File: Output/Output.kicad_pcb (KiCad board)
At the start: 2 copper layers, 118 x 51.5 mm, 22 parts, among them J1 Conn_01x10_Pin, J2 Conn_01x04_Pin, J3 Conn_01x03_Pin, J4 Conn_01x02_Pin, J5 Conn_01x01_Pin, U10 HDSP-7403, U11 ATMEGA328-PU, U2 74LS273, U3 74HC595, U4 HDSP-7403, U5 74HC595, U6 HDSP-7403, U7 74HC595, U8 HDSP-7403, U9 74HC595, Y1 16MHz

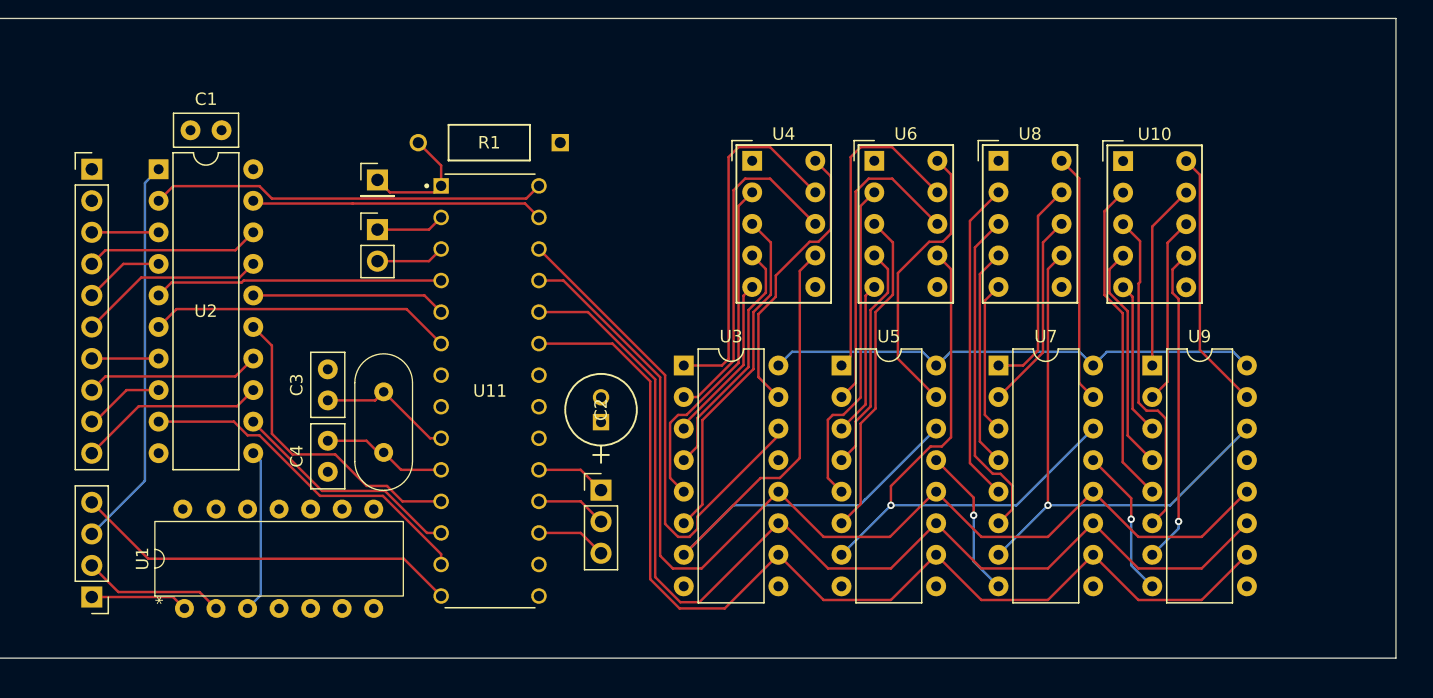
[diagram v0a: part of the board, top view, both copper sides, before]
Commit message: Output PCB routed
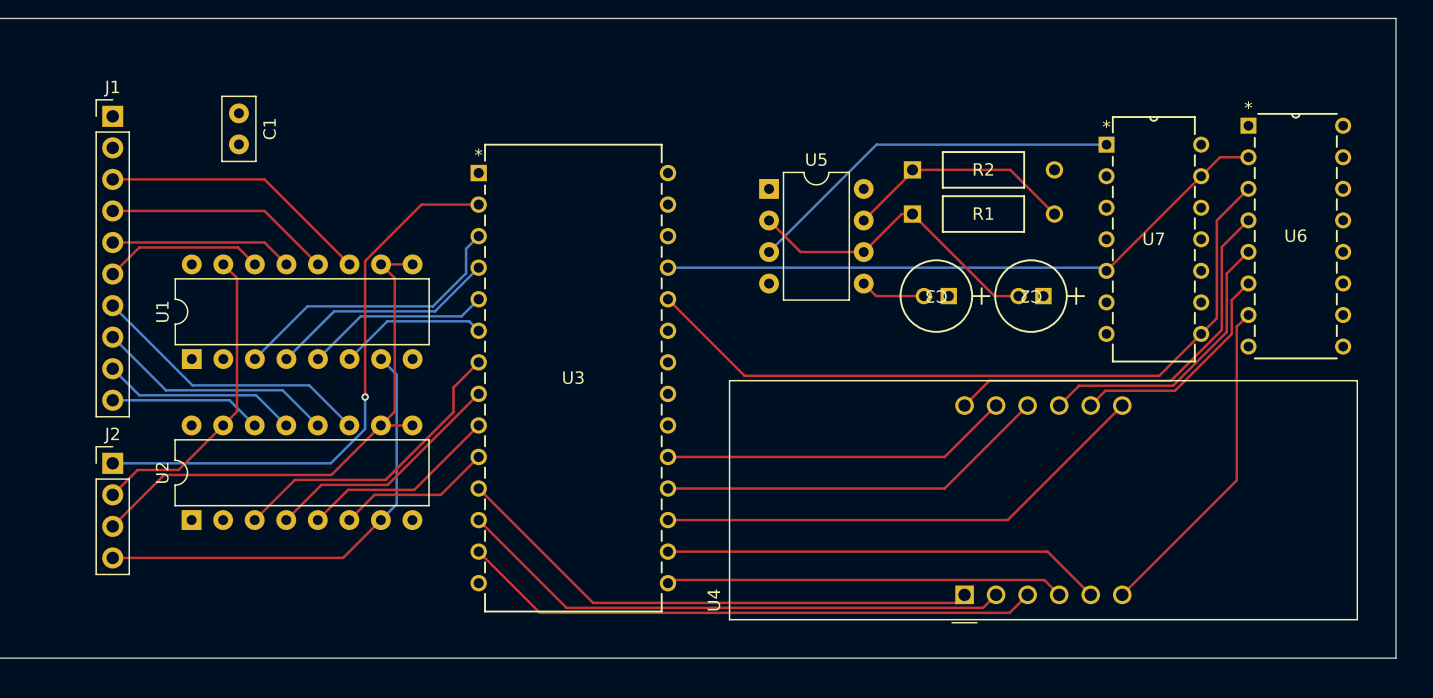
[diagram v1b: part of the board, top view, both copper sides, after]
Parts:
- removed C4: 22pF, Capacitor_THT:C_Disc_D5.0mm_W2.5mm_P2.50mm
- removed J3: Conn_01x03_Pin, Connector_PinHeader_2.54mm:PinHeader_1x03_P2.54mm_Vertical
- removed J4: Conn_01x02_Pin, Connector_PinHeader_2.54mm:PinHeader_1x02_P2.54mm_Vertical
- removed J5: Conn_01x01_Pin, Connector_PinHeader_2.54mm:PinHeader_1x01_P2.54mm_Vertical
- removed U10, U8: HDSP-7403, Display_7Segment:HDSP-7401
- removed U11: ATMEGA328-PU, _DownloadFootprints:DIP787W46P254L3467H508Q28
- removed U9: 74HC595, Package_DIP:DIP-16_W7.62mm
- removed Y1: 16MHz, 8BitCPUFootprints:16MHzCrystalOscillator
- added R2: 1k, _DownloadFootprints:CF_series_Resistors_THT, F.Cu at (155.6, 75.7)
- C2: value 0.1uF -> 0.01u
- C3: value 22pF -> 0.01u; footprint Capacitor_THT:C_Disc_D5.0mm_W2.5mm_P2.50mm -> _DownloadFootprints:Cp_2mm_pin_spacing
- R1: value 10k -> 100k
- U1: value ~ -> 74LS173; footprint 8BitCPUFootprints:4x_and -> Package_DIP:DIP-16_W7.62mm
- U2: value 74LS273 -> 74LS173; footprint Package_DIP:DIP-20_W7.62mm -> Package_DIP:DIP-16_W7.62mm
- U3: value 74HC595 -> AT28C64B-15PI; footprint Package_DIP:DIP-16_W7.62mm -> _DownloadFootprints:eeprom
- U4: value HDSP-7403 -> CC56-12CGKWA; footprint Display_7Segment:HDSP-7401 -> Display_7Segment:CA56-12CGKWA
- U5: value 74HC595 -> NE555P; footprint Package_DIP:DIP-16_W7.62mm -> Package_DIP:DIP-8_W7.62mm
- U6: value HDSP-7403 -> CD74HCT139E; footprint Display_7Segment:HDSP-7401 -> _DownloadFootprints:2x_2_to_4_demux
- U7: value 74HC595 -> CD74HCT73E; footprint Package_DIP:DIP-16_W7.62mm -> _DownloadFootprints:2x_JK_FF
- moved C3 50.7 mm to (158.5, 85.9), turned to 180 degrees
- moved U6 40.6 mm to (190.2, 89.9)
- moved U4 38.9 mm to (159.8, 109.9), turned to 90 degrees
- moved C2 37.0 mm to (166.1, 85.9), turned to 180 degrees
- moved R1 28.9 mm to (155.6, 79.2), turned to 0 degrees
- moved U2 28.4 mm to (97.5, 103.9), turned to 90 degrees
- moved U3 17.6 mm to (135.9, 109.0)
- moved U1 17.5 mm to (97.6, 90.9)
- moved U7 16.5 mm to (178.8, 88.9)
- moved U5 15.4 mm to (144.0, 77.2)
- moved J2 10.9 mm to (91.2, 99.3), turned to 0 degrees
- moved J1 4.58 mm to (91.2, 71.4)
- moved C1 4.13 mm to (101.3, 71.1), turned to -90 degrees
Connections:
- C2 pad 1: +5V -> GND
- C2 pad 2: GND -> Net-(U5-THR)
- C3 pad 1: /MCU/XTAL1 -> GND
- C3 pad 2: GND -> Net-(U5-CV)
- J2 pad 1: /CLK -> /2's Comp
- J2 pad 2: /En -> /RST
- J2 pad 3: /~{RST} -> /~{En}
- J2 pad 4: /2's Comp -> /CLK
- R1 pad 1: +5V -> Net-(U5-THR)
- R1 pad 2: /MCU/RST -> Net-(U5-DIS)
- U1 pad 1: /CLK -> GND
- U1 pad 10: unconnected-(U1-3B-Pad10) -> /~{En}
- U1 pad 11: unconnected-(U1-4Y-Pad11) -> /Bus 0
- U1 pad 12: unconnected-(U1-4A-Pad12) -> /Bus 1
- U1 pad 13: unconnected-(U1-4B-Pad13) -> /Bus 2
- U1 pad 14: +5V -> /Bus 3
- U1 pad 2: /En -> GND
- U1 pad 3: Net-(U1-1Y) -> /D3
- U1 pad 4: unconnected-(U1-2A-Pad4) -> /D2
- U1 pad 5: unconnected-(U1-2B-Pad5) -> /D1
- U1 pad 6: unconnected-(U1-2Y-Pad6) -> /D0
- U1 pad 7: GND -> /CLK
- U1 pad 8: unconnected-(U1-3Y-Pad8) -> GND
- U1 pad 9: unconnected-(U1-3A-Pad9) -> /~{En}
- U2 pad 1: /~{RST} -> GND
- U2 pad 10: GND -> /~{En}
- U2 pad 11: Net-(U1-1Y) -> /Bus 4
- U2 pad 12: /D7 -> /Bus 5
- U2 pad 13: /Bus 7 -> /Bus 6
- U2 pad 14: /Bus 5 -> /Bus 7
- U2 pad 15: /D5 -> /RST
- U2 pad 16: /D3 -> +5V
- U2 pad 2: /D0 -> GND
- U2 pad 3: /Bus 0 -> /D7
- U2 pad 4: /Bus 2 -> /D6
- U2 pad 5: /D2 -> /D5
- U2 pad 7: /Bus 4 -> /CLK
- U2 pad 8: /Bus 6 -> GND
- U2 pad 9: /D6 -> /~{En}
- U3 pad 1: Net-(U3-QB) -> unconnected-(U3-NC-Pad1)
- U3 pad 10: /MCU/~{Display RST} -> /D4
- U3 pad 11: /MCU/SR_CLK -> /e
- U3 pad 12: /MCU/Latch -> /d
- U3 pad 13: GND -> /dp
- U3 pad 14: /MCU/SER_IN -> GND
- U3 pad 15: Net-(U3-QA) -> /c
- U3 pad 16: +5V -> /g
- U3 pad 2: Net-(U3-QC) -> /2's Comp
- U3 pad 3: Net-(U3-QD) -> /D3
- U3 pad 4: Net-(U3-QE) -> /D2
- U3 pad 5: Net-(U3-QF) -> /D1
- U3 pad 6: Net-(U3-QG) -> /D0
- U3 pad 7: /OutputDisplay/7SegmentShiftRegister/SER_OUT -> /D7
- U3 pad 8: GND -> /D6
- U3 pad 9: unconnected-(U3-QH'-Pad9) -> /D5
- U4 pad 1: GND -> /e
- U4 pad 10: Net-(U3-QA) -> /f
- U4 pad 2: Net-(U3-QF) -> /d
- U4 pad 3: Net-(U3-QG) -> /dp
- U4 pad 4: Net-(U3-QE) -> /c
- U4 pad 5: Net-(U3-QD) -> /g
- U4 pad 6: GND -> /DT3
- U4 pad 7: /OutputDisplay/7SegmentShiftRegister/SER_OUT -> /b
- U4 pad 8: Net-(U3-QC) -> /DT2
- U4 pad 9: Net-(U3-QB) -> /DT1
- U5 pad 1: Net-(U5-QB) -> GND
- U5 pad 2: Net-(U5-QC) -> Net-(U5-THR)
- U5 pad 3: Net-(U5-QD) -> Net-(U5-Q)
- U5 pad 4: Net-(U5-QE) -> unconnected-(U5-R-Pad4)
- U5 pad 5: Net-(U5-QF) -> Net-(U5-CV)
- U5 pad 6: Net-(U5-QG) -> Net-(U5-THR)
- U5 pad 7: /OutputDisplay/7SegmentShiftRegister1/SER_OUT -> Net-(U5-DIS)
- U5 pad 8: GND -> +5V
- U6 pad 1: GND -> +5V
- U6 pad 10: Net-(U5-QA) -> unconnected-(U6-*2Y2-Pad10)
- U6 pad 2: Net-(U5-QF) -> /~{Q1}
- U6 pad 3: Net-(U5-QG) -> /~{Q2}
- U6 pad 4: Net-(U5-QE) -> /DT0
- U6 pad 5: Net-(U5-QD) -> /DT1
- U6 pad 6: GND -> /DT2
- U6 pad 7: /OutputDisplay/7SegmentShiftRegister1/SER_OUT -> /DT3
- U6 pad 8: Net-(U5-QC) -> GND
- U6 pad 9: Net-(U5-QB) -> unconnected-(U6-*2Y3-Pad9)
- U7 pad 1: Net-(U7-QB) -> Net-(U5-Q)
- U7 pad 10: /MCU/~{Display RST} -> +5V
- U7 pad 11: /MCU/SR_CLK -> GND
- U7 pad 12: /MCU/Latch -> unconnected-(U7-1Q-Pad12)
- U7 pad 13: GND -> /~{Q1}
- U7 pad 14: /OutputDisplay/7SegmentShiftRegister1/SER_OUT -> +5V
- U7 pad 2: Net-(U7-QC) -> +5V
- U7 pad 3: Net-(U7-QD) -> +5V
- U7 pad 4: Net-(U7-QE) -> +5V
- U7 pad 5: Net-(U7-QF) -> /~{Q1}
- U7 pad 6: Net-(U7-QG) -> +5V
- U7 pad 7: /OutputDisplay/7SegmentShiftRegister2/SER_OUT -> +5V
- U7 pad 8: GND -> /~{Q2}
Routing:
- net /MCU/SR_CLK: track 87.7 -> 0.00 mm
- net /MCU/Latch: track 86.6 -> 0.00 mm
- net /MCU/~{Display RST}: track 86.0 -> 0.00 mm
- net /~{Q2}: track 0.00 -> 60.1 mm
- net /OutputDisplay/7SegmentShiftRegister/SER_OUT: track 53.9 -> 0.00 mm
- net /~{Q1}: track 0.00 -> 50.6 mm
- net /OutputDisplay/7SegmentShiftRegister1/SER_OUT: track 47.6 -> 0.00 mm, vias 1 -> 0
- net /dp: track 0.00 -> 46.8 mm
- net /d: track 0.00 -> 45.0 mm
- net /OutputDisplay/7SegmentShiftRegister2/SER_OUT: track 44.8 -> 0.00 mm, vias 1 -> 0
- net /~{En}: track 0.00 -> 43.9 mm
- net /e: track 0.00 -> 43.2 mm
- net +5V: track 40.5 -> 0.00 mm
- net /MCU/SER_IN: track 40.4 -> 0.00 mm
- net /b: track 0.00 -> 40.4 mm
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
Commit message: Added silkscreen to IO and added edge cuts and mounting points
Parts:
- added REF**: MountingHole_2.2mm_M2, MountingHole:MountingHole_2.2mm_M2, F.Cu at (90.5, 113.8)
- added REF**: MountingHole_2.2mm_M2, MountingHole:MountingHole_2.2mm_M2, F.Cu at (193.5, 66.9)
- added REF**: MountingHole_2.2mm_M2, MountingHole:MountingHole_2.2mm_M2, F.Cu at (193.5, 113.8)
- added REF**: MountingHole_2.2mm_M2, MountingHole:MountingHole_2.2mm_M2, F.Cu at (90.5, 66.9)
- C2, C3: footprint _DownloadFootprints:Cp_2mm_pin_spacing -> Capacitor_THT:C_Disc_D5.0mm_W2.5mm_P2.50mm
- moved C3 12.3 mm to (146.6, 88.8), turned to 0 degrees
- moved C2 11.3 mm to (155.1, 88.2), turned to 90 degrees
- moved C1 2.55 mm to (98.8, 71.4)
- moved J1 0.76 mm to (90.4, 71.4)
- moved J2 0.76 mm to (90.4, 99.3)
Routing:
- net Net-(U5-THR): track 25.1 -> 18.7 mm
- net /Bus 6: track 15.9 -> 16.6 mm
- net /~{En}: track 43.9 -> 44.7 mm
- net /RST: track 25.1 -> 25.8 mm
- net /CLK: track 36.9 -> 37.6 mm
- net /Bus 7: track 12.3 -> 13.0 mm
- net /Bus 5: track 19.5 -> 20.2 mm
- net /Bus 4: track 23.0 -> 23.8 mm
- net /Bus 3: track 12.9 -> 13.7 mm
- net /Bus 2: track 14.7 -> 15.5 mm
- net /Bus 1: track 18.3 -> 19.1 mm
- net /Bus 0: track 21.9 -> 22.7 mm
- net /2's Comp: track 46.0 -> 46.8 mm
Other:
- board size 118 x 51.5 mm -> 109 x 52.9 mm
- board text added: "2C"
- board text added: "B0"
- board text added: "B1"
- board text added: "B2"
- board text added: "B3"
- board text added: "B4"
- board text added: "B5"
- board text added: "B6"
- board text added: "B7"
- board text added: "CLK"
- board text added: "GND"
- board text added: "Output"
- board text added: "RST"
- board text added: "VCC"
- board text added: "~{EN}"

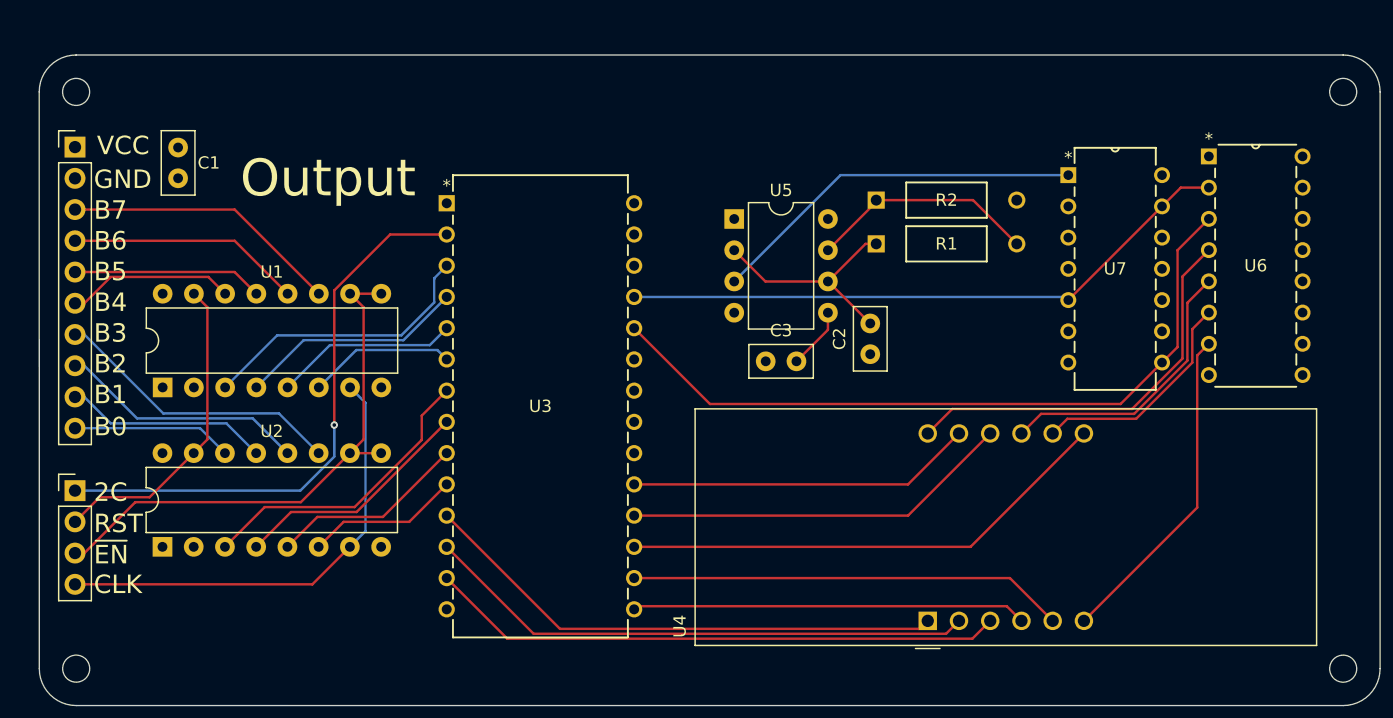
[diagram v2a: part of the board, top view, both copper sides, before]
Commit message: Minor updates to layout and silk screen
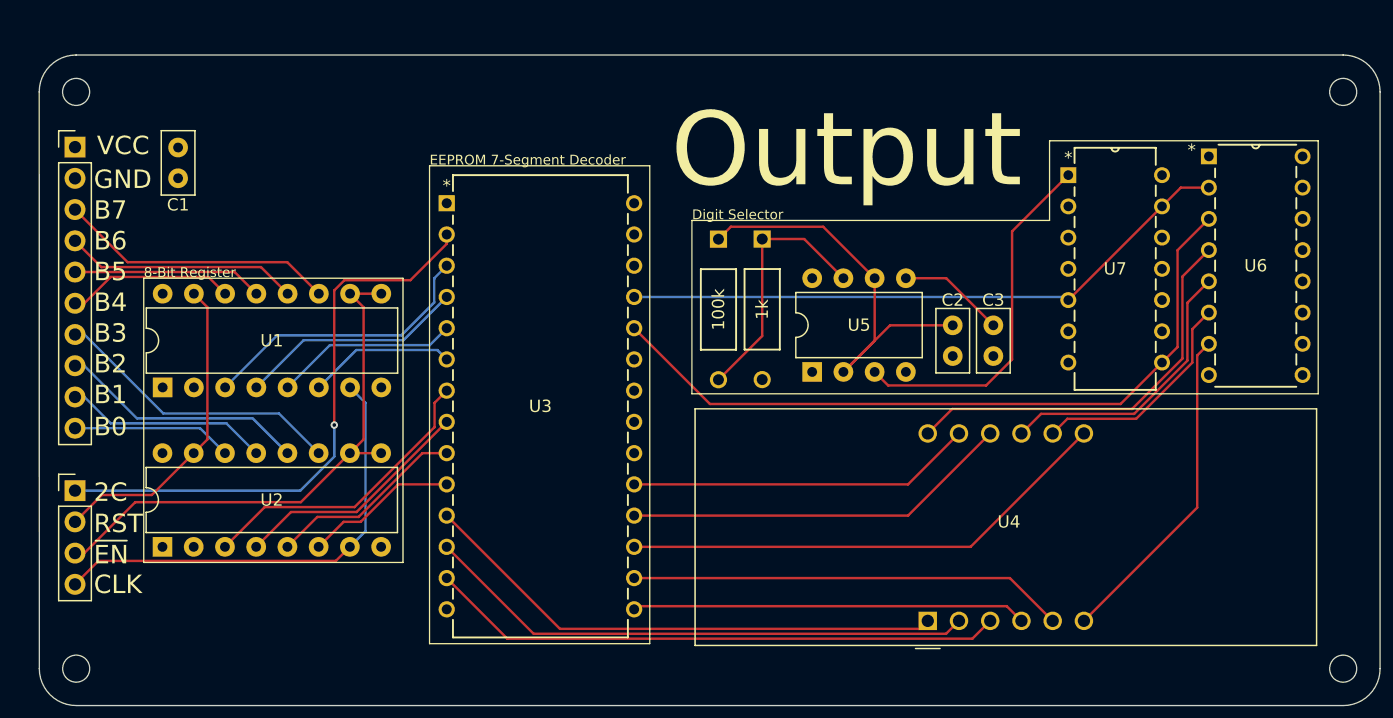
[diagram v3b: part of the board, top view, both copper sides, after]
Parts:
- moved C3 18.5 mm to (165.1, 88.4), turned to 90 degrees
- moved U5 14.0 mm to (150.4, 89.7), turned to 90 degrees
- moved R1 12.8 mm to (142.7, 78.9), turned to -90 degrees
- moved R2 9.80 mm to (146.3, 78.9), turned to -90 degrees
- moved C2 6.71 mm to (161.8, 88.4)
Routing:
- net Net-(U5-THR): track 18.7 -> 34.0 mm
- net Net-(U5-CV): track 5.01 -> 8.70 mm
- net Net-(U5-DIS): track 18.6 -> 20.8 mm
- net Net-(U5-Q): track 30.7 -> 29.4 mm
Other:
- board text added: "100k"
- board text added: "1k"
- board text added: "8-Bit Register"
- board text added: "Digit Selector"
- board text added: "EEPROM 7-Segment Decoder"
